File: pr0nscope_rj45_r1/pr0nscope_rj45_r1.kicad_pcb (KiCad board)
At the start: 2 copper layers, 165 x 160 mm, 25 parts, among them J1 Conn_01x01, J2 RJ45-index, J3 pr0nscope_db25f_gnd, J4 Conn_01x01, J5 RJ45-index, J6 pr0nscope_db25f_gnd, J7 Conn_01x02, J8 Conn_02x03_Odd_Even, U1 L7805

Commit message: pr0nscope_rj45_r1_rc1
Signed-off-by: John McMaster <johndmcmaster@gmail.com>
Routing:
- net VDD: track 413.5 -> 350.5 mm, vias 7 -> 4
- net GND: track 502.6 -> 514.1 mm
- net +5V: track 281.1 -> 279.5 mm
- net Net-(J5-Pad7): track 159.6 -> 159.7 mm, vias 2 -> 4
- net Net-(J2-Pad1): vias 2 -> 4
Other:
- board text added: "HIDE ME!"
- board text added: "John McMaster 2018"
- board text added: "pr0nscope_rj45_r1"

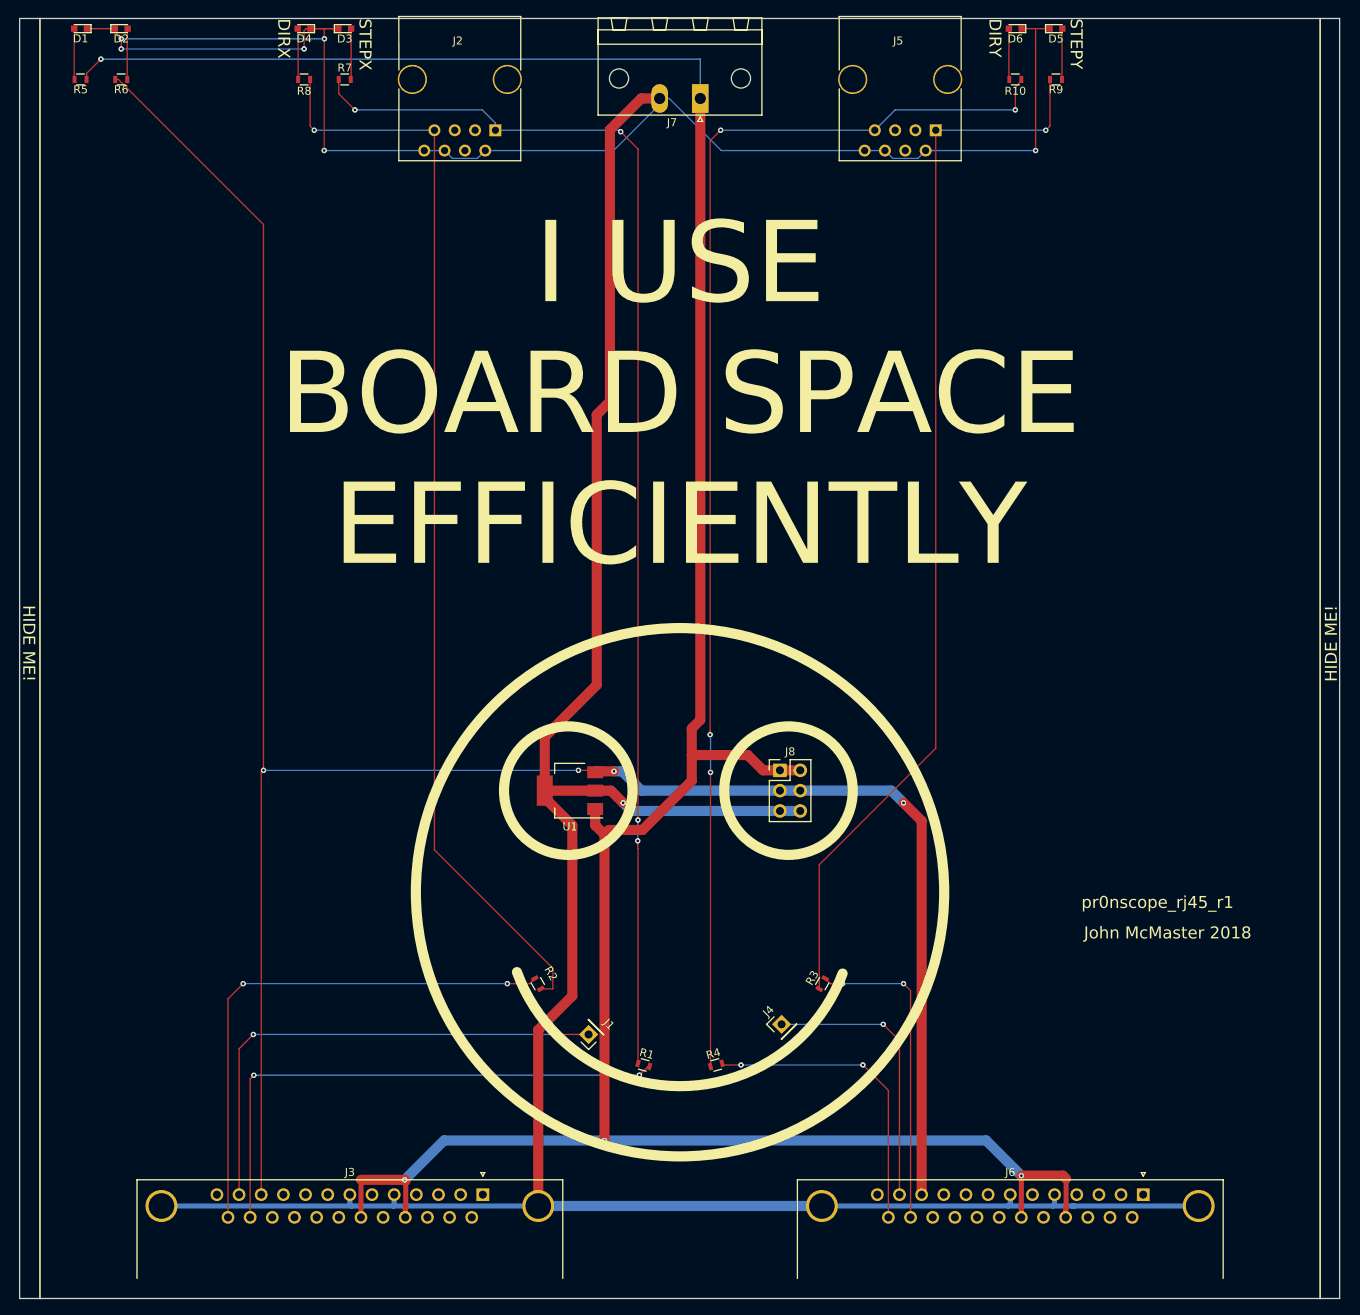
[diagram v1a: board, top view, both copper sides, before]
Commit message: pr0nscope_rj45_r1 rc2: increase power via size
Signed-off-by: John McMaster <johndmcmaster@gmail.com>
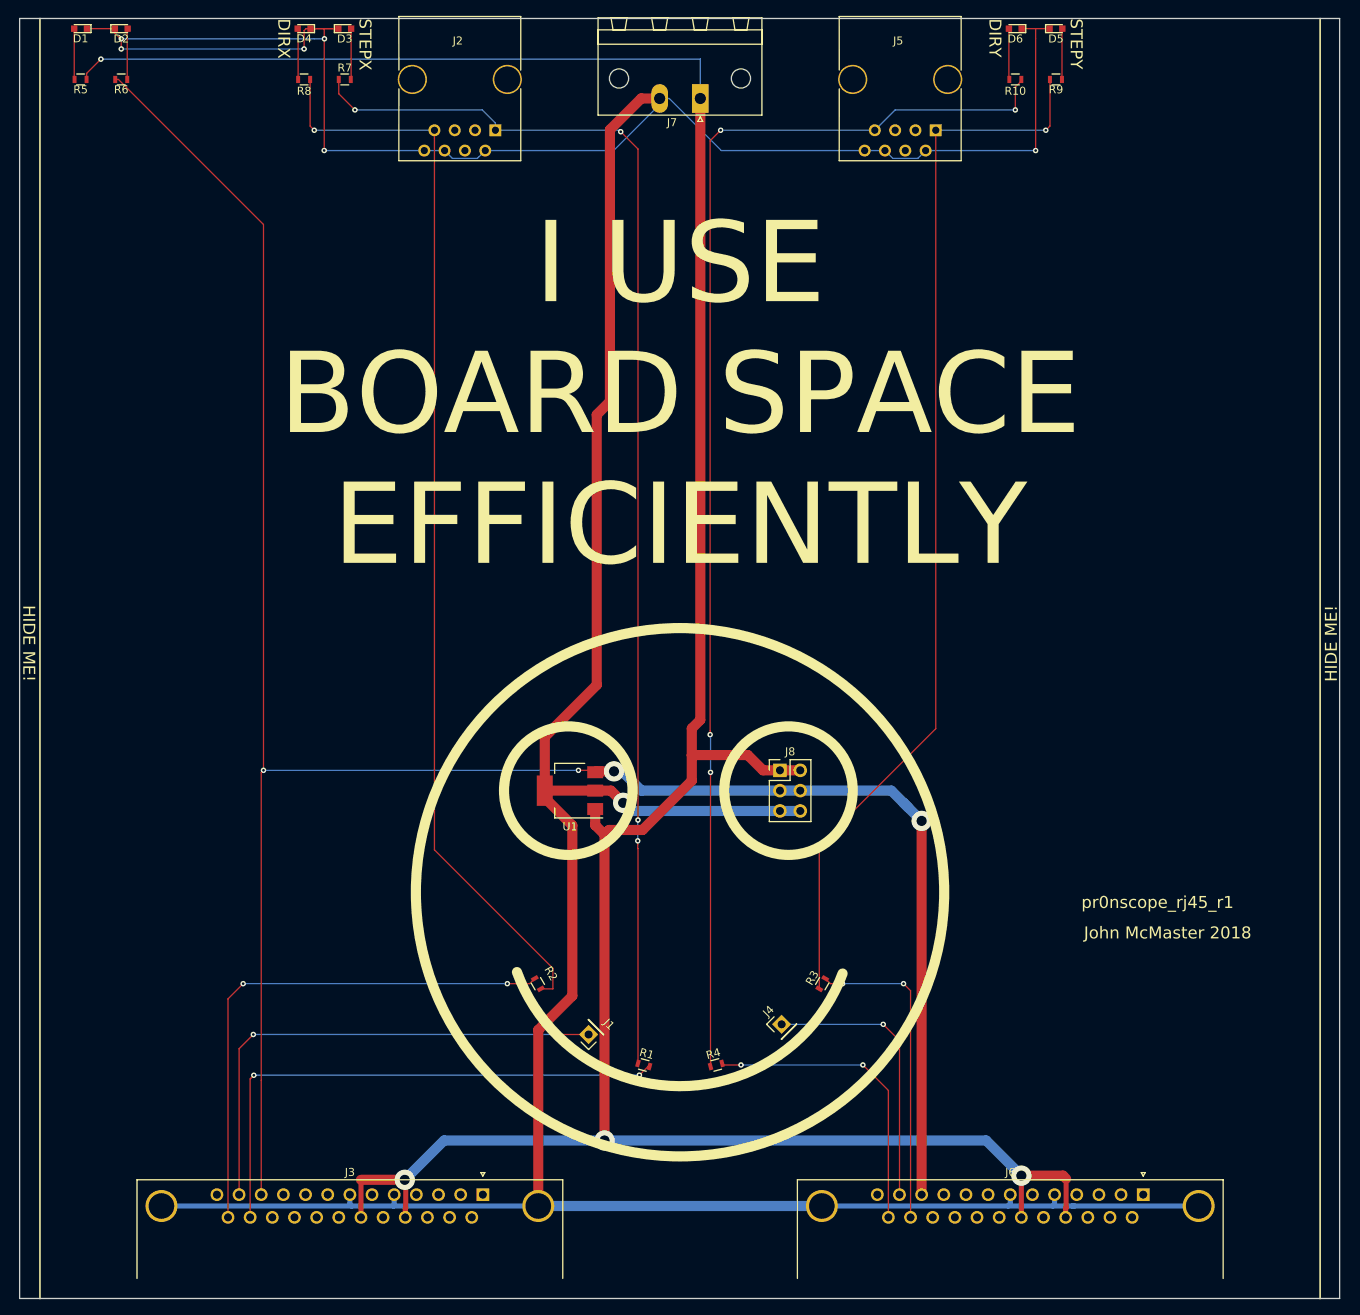
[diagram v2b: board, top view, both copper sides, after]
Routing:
- net +5V: track 279.5 -> 280.4 mm
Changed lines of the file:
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@@
     (links 57)
     (no_connects 0)
-    (area 25.398729 25.398729 190.401271 185.401271)
+    (area 25.193 24.722599 190.707 192.0574)
     (thickness 1.6)
     (drawings 19)
-    (tracks 255)
+    (tracks 257)
     (zones 0)
     (modules 25)
@@
     (via_min_size 0.508)
     (via_min_drill 0.254)
+    (user_via 0.6858 0.3302)
+    (user_via 5.08 2.54)
     (uvia_size 0.6858)
     (uvia_drill 0.3302)
@@
   (segment (start 97.341666 121.92) (end 99.314 121.92) (width 1.27) (layer F.Cu) (net 2))
   (segment (start 99.314 121.92) (end 100.838 123.444) (width 1.27) (layer F.Cu) (net 2))
-  (via (at 100.838 123.444) (size 0.6858) (drill 0.3302) (layers F.Cu B.Cu) (net 2))
+  (via (at 100.838 123.444) (size 2.54) (drill 1.27) (layers F.Cu B.Cu) (net 2))
   (segment (start 91.041666 121.92) (end 97.341666 121.92) (width 1.27) (layer F.Cu) (net 2))
   (segment (start 94.488 126.266334) (end 91.041666 122.82) (width 1.27) (layer F.Cu) (net 2))
@@
   (segment (start 61.71 38.85) (end 62.23 39.37) (width 0.1524) (layer F.Cu) (net 13))
   (via (at 62.23 39.37) (size 0.6858) (drill 0.3302) (layers F.Cu B.Cu) (net 13))
+  (segment (start 135.89 123.444) (end 138.149998 125.703998) (width 1.27) (layer B.Cu) (net 22))
+  (via (at 138.149998 125.703998) (size 2.54) (drill 1.27) (layers F.Cu B.Cu) (net 22))
+  (segment (start 135.89 123.444) (end 136.525 124.079) (width 1.27) (layer B.Cu) (net 22))
+  (segment (start 134.366 121.92) (end 135.89 123.444) (width 1.27) (layer B.Cu) (net 22))
   (segment (start 99.695 119.507) (end 97.454666 119.507) (width 1.27) (layer F.Cu) (net 22))
   (segment (start 97.454666 119.507) (end 97.341666 119.62) (width 1.27) (layer F.Cu) (net 22))
   (segment (start 103.124 121.92) (end 100.711 119.507) (width 1.27) (layer B.Cu) (net 22))
   (segment (start 100.711 119.507) (end 99.695 119.507) (width 1.27) (layer B.Cu) (net 22))
-  (via (at 99.695 119.507) (size 0.6858) (drill 0.3302) (layers F.Cu B.Cu) (net 22))
+  (via (at 99.695 119.507) (size 2.54) (drill 1.27) (layers F.Cu B.Cu) (net 22))
   (segment (start 120.438332 121.92) (end 103.124 121.92) (width 1.27) (layer B.Cu) (net 22))
-  (segment (start 135.89 123.444) (end 138.149998 125.703998) (width 1.27) (layer F.Cu) (net 22))
   (segment (start 138.149998 125.703998) (end 138.149998 172.42) (width 1.27) (layer F.Cu) (net 22))
   (segment (start 122.978332 121.92) (end 134.366 121.92) (width 1.27) (layer B.Cu) (net 22))
-  (segment (start 134.366 121.92) (end 135.89 123.444) (width 1.27) (layer B.Cu) (net 22))
-  (via (at 135.89 123.444) (size 0.6858) (drill 0.3302) (layers F.Cu B.Cu) (net 22))
   (segment (start 120.438332 121.92) (end 122.978332 121.92) (width 1.27) (layer B.Cu) (net 22))
   (segment (start 55.88 119.38) (end 55.88 51.1476) (width 0.1524) (layer F.Cu) (net 22))
@@
   (segment (start 55.6 172.42) (end 55.6 158.134573) (width 0.1524) (layer F.Cu) (net 22))
   (segment (start 97.581666 119.38) (end 97.341666 119.62) (width 0.1524) (layer F.Cu) (net 22))
+  (segment (start 98.509492 127.407826) (end 98.509492 165.650508) (width 1.27) (layer F.Cu) (net 27))
   (segment (start 120.438332 119.38) (end 122.978332 119.38) (width 1.27) (layer F.Cu) (net 27))
   (segment (start 109.41757 117.475) (end 109.41757 120.681912) (width 1.27) (layer F.Cu) (net 27))
@@
   (segment (start 98.509492 165.650508) (end 146.219508 165.650508) (width 1.27) (layer B.Cu) (net 27))
   (segment (start 146.219508 165.650508) (end 150.614998 170.045998) (width 1.27) (layer B.Cu) (net 27))
-  (via (at 150.614998 170.045998) (size 0.6858) (drill 0.3302) (layers F.Cu B.Cu) (net 27))
+  (via (at 150.614998 170.045998) (size 2.54) (drill 1.27) (layers F.Cu B.Cu) (net 27))
   (segment (start 98.509492 165.650508) (end 78.457492 165.650508) (width 1.27) (layer B.Cu) (net 27))
   (segment (start 78.457492 165.650508) (end 73.54 170.568) (width 1.27) (layer B.Cu) (net 27))
-  (via (at 73.54 170.568) (size 0.6858) (drill 0.3302) (layers F.Cu B.Cu) (net 27))
-  (via (at 98.509492 165.650508) (size 0.6858) (drill 0.3302) (layers F.Cu B.Cu) (net 27))
+  (via (at 73.54 170.568) (size 2.54) (drill 1.27) (layers F.Cu B.Cu) (net 27))
+  (via (at 98.509492 165.650508) (size 2.54) (drill 1.27) (layers F.Cu B.Cu) (net 27))
   (segment (start 97.341666 124.22) (end 97.341666 126.24) (width 1.27) (layer F.Cu) (net 27))
   (segment (start 97.341666 126.24) (end 98.509492 127.407826) (width 1.27) (layer F.Cu) (net 27))
-  (segment (start 98.509492 127.407826) (end 98.509492 165.650508) (width 1.27) (layer F.Cu) (net 27))
   (segment (start 155.821998 170.045998) (end 156.21 170.434) (width 1.27) (layer F.Cu) (net 27))
   (segment (start 156.21 174.073628) (end 156.21 170.434) (width 0.635) (layer F.Cu) (net 27))
@@
   (segment (start 135.379998 153.159998) (end 133.35 151.13) (width 0.1524) (layer F.Cu) (net 35))
   (via (at 133.35 151.13) (size 0.6858) (drill 0.3302) (layers F.Cu B.Cu) (net 35))
-  (segment (start 139.916666 116.623334) (end 125.355 131.185) (width 0.1524) (layer F.Cu) (net 36))
-  (segment (start 125.355 131.185) (end 125.355 146.699519) (width 0.1524) (layer F.Cu) (net 36))
-  (segment (start 139.916666 39.37) (end 139.916666 116.623334) (width 0.1524) (layer F.Cu) (net 36))
+  (segment (start 125.355 146.310845) (end 125.355 146.699519) (width 0.1524) (layer F.Cu) (net 36))
+  (segment (start 125.355 128.73847) (end 125.355 146.310845) (width 0.1524) (layer F.Cu) (net 36))
+  (segment (start 139.916666 114.176804) (end 125.355 128.73847) (width 0.1524) (layer F.Cu) (net 36))
+  (segment (start 139.916666 39.37) (end 139.916666 114.176804) (width 0.1524) (layer F.Cu) (net 36))
   (segment (start 153.67 39.37) (end 139.916666 39.37) (width 0.1524) (layer B.Cu) (net 36))
   (segment (start 154.19 33.02) (end 154.19 38.85) (width 0.1524) (layer F.Cu) (net 36))
